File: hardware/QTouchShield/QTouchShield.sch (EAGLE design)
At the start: 114 parts, among them IC1 AT32UC3C0512CJEDEC-MS-026, U1 ARDUINO-MEGALITE

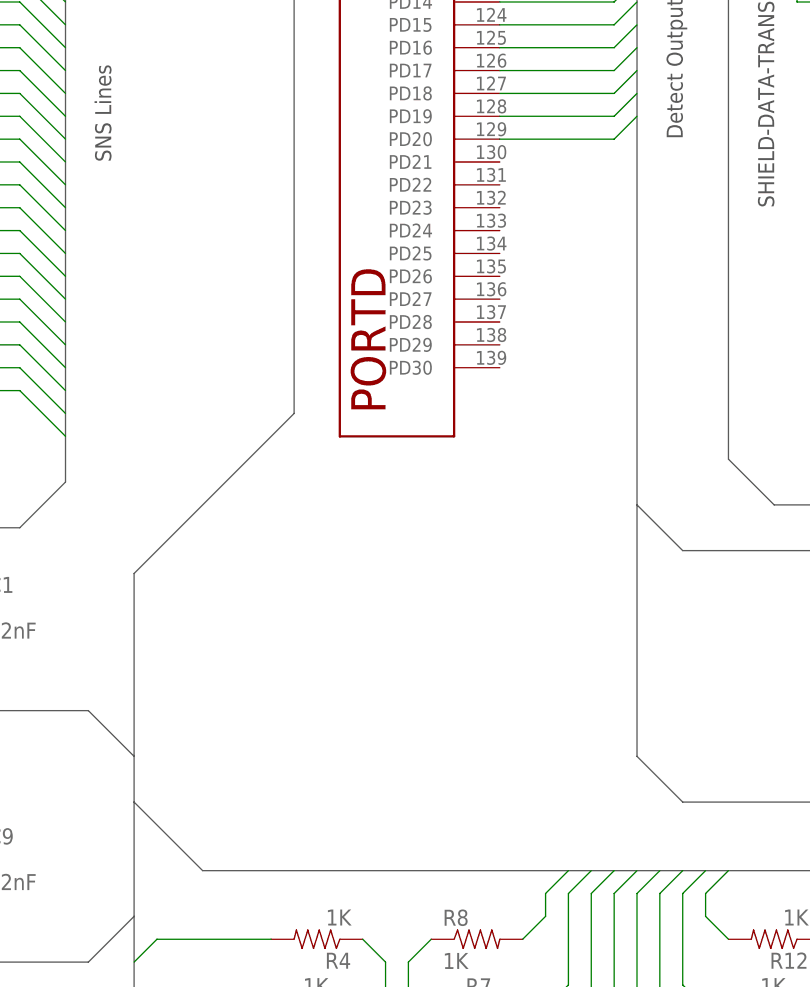
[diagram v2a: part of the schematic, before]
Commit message: Added TOUCH DATA header for data transfer to QT600 Interface Board
TOUCH DATA header added. This is the bit-banged SPI interface for
transferring debug data to the QT600 board for analysing touch data
with QTouch Studio.
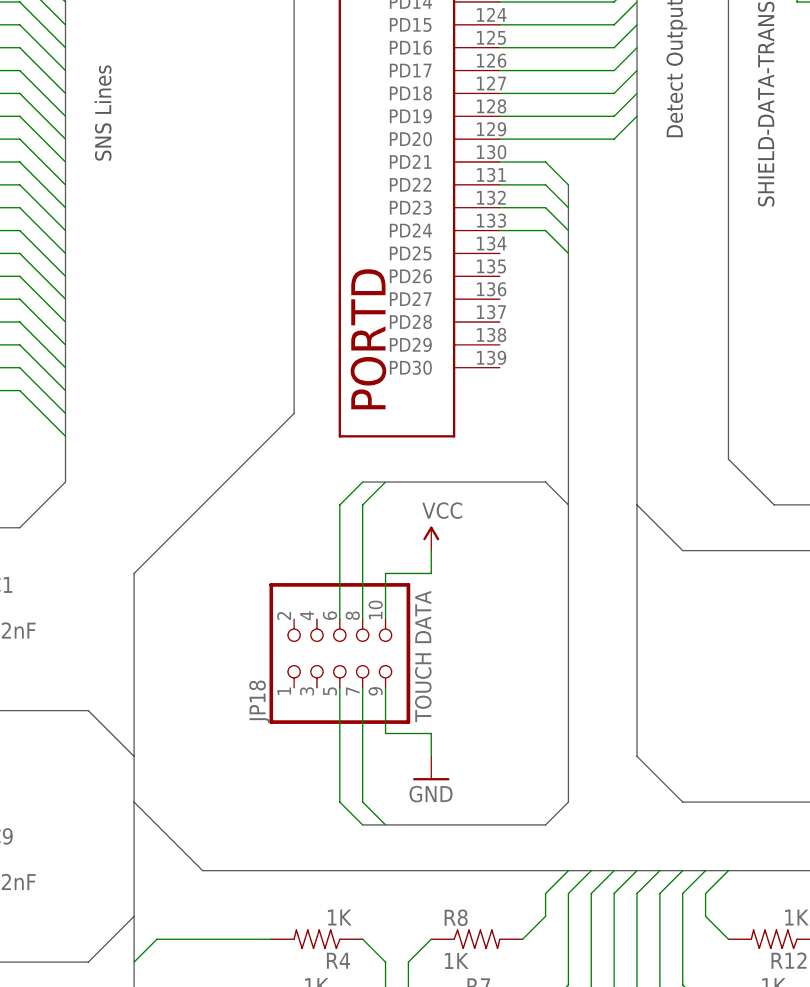
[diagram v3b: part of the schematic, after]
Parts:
- added JP18: TOUCH DATA, pinhead:PINHD-2X5
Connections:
- new net TOUCH_DATA-MISO: IC1.PD24, JP18.7
- new net TOUCH_DATA-MOSI: IC1.PD23, JP18.6
- new net TOUCH_DATA-SCK: IC1.PD22, JP18.8
- new net TOUCH_DATA-SS: IC1.PD21, JP18.5
- net GND: now also JP18.9
- net VCC: now also JP18.10
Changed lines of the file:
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@@
 <layers>
 <layer number="1" name="Top" color="4" fill="1" visible="no" active="no"/>
+<layer number="2" name="Route2" color="1" fill="3" visible="no" active="no"/>
+<layer number="3" name="Route3" color="4" fill="3" visible="no" active="no"/>
+<layer number="14" name="Route14" color="1" fill="6" visible="no" active="no"/>
+<layer number="15" name="Route15" color="4" fill="6" visible="no" active="no"/>
 <layer number="16" name="Bottom" color="1" fill="1" visible="no" active="no"/>
 <layer number="17" name="Pads" color="2" fill="1" visible="no" active="no"/>
@@
 <part name="R35" library="SparkFun" deviceset="RESISTOR" device="0805-RES" value="10K"/>
 <part name="SJ5" library="jumper" deviceset="SJ" device="" value="RESET-LINK"/>
+<part name="JP18" library="pinhead" deviceset="PINHD-2X5" device="" value="TOUCH DATA"/>
+<part name="GND9" library="SparkFun" deviceset="GND" device=""/>
+<part name="P+6" library="SparkFun" deviceset="VCC" device=""/>
 </parts>
 <sheets>
@@
 <attribute name="VALUE" x="194.31" y="40.64" size="1.778" layer="96" rot="R270"/>
 </instance>
+<instance part="JP18" gate="A" x="116.84" y="-139.7" rot="R90"/>
+<instance part="GND9" gate="1" x="127" y="-152.4"/>
+<instance part="P+6" gate="1" x="127" y="-127"/>
 </instances>
 <busses>
@@
 </segment>
 </bus>
+<bus name="TOUCH_DATA-SS,TOUCH_DATA-SCK,TOUCH_DATA-MOSI,TOUCH_DATA-MISO">
+<segment>
+<wire x1="142.24" y1="-86.36" x2="142.24" y2="-121.92" width="0.762" layer="92"/>
+<wire x1="142.24" y1="-121.92" x2="139.7" y2="-119.38" width="0.762" layer="92"/>
+<wire x1="139.7" y1="-119.38" x2="119.38" y2="-119.38" width="0.762" layer="92"/>
+<wire x1="142.24" y1="-121.92" x2="142.24" y2="-154.94" width="0.762" layer="92"/>
+<wire x1="142.24" y1="-154.94" x2="139.7" y2="-157.48" width="0.762" layer="92"/>
+<wire x1="139.7" y1="-157.48" x2="119.38" y2="-157.48" width="0.762" layer="92"/>
+</segment>
+</bus>
 </busses>
 <nets>
@@
 <wire x1="-22.86" y1="-40.64" x2="-22.86" y2="-38.1" width="0.1524" layer="91"/>
 </segment>
+<segment>
+<pinref part="GND9" gate="1" pin="GND"/>
+<wire x1="127" y1="-149.86" x2="127" y2="-147.32" width="0.1524" layer="91"/>
+<wire x1="127" y1="-147.32" x2="121.92" y2="-147.32" width="0.1524" layer="91"/>
+<pinref part="JP18" gate="A" pin="9"/>
+<wire x1="121.92" y1="-147.32" x2="121.92" y2="-142.24" width="0.1524" layer="91"/>
+</segment>
 </net>
 <net name="N$2" class="0">
@@
 <wire x1="-12.7" y1="20.32" x2="-12.7" y2="22.86" width="0.1524" layer="91"/>
 </segment>
+<segment>
+<pinref part="P+6" gate="1" pin="VCC"/>
+<wire x1="127" y1="-127" x2="127" y2="-129.54" width="0.1524" layer="91"/>
+<wire x1="127" y1="-129.54" x2="121.92" y2="-129.54" width="0.1524" layer="91"/>
+<pinref part="JP18" gate="A" pin="10"/>
+<wire x1="121.92" y1="-129.54" x2="121.92" y2="-134.62" width="0.1524" layer="91"/>
+</segment>
 </net>
 <net name="JTAG_TMS" class="0">
@@
 </segment>
 </net>
+<net name="TOUCH_DATA-SS" class="0">
+<segment>
+<wire x1="142.24" y1="-86.36" x2="139.7" y2="-83.82" width="0.1524" layer="91"/>
+<pinref part="IC1" gate="G$1" pin="PD21"/>
+<wire x1="139.7" y1="-83.82" x2="134.62" y2="-83.82" width="0.1524" layer="91"/>
+</segment>
+<segment>
+<wire x1="119.38" y1="-157.48" x2="116.84" y2="-154.94" width="0.1524" layer="91"/>
+<pinref part="JP18" gate="A" pin="5"/>
+<wire x1="116.84" y1="-154.94" x2="116.84" y2="-142.24" width="0.1524" layer="91"/>
+</segment>
+</net>
+<net name="TOUCH_DATA-SCK" class="0">
+<segment>
+<wire x1="142.24" y1="-88.9" x2="139.7" y2="-86.36" width="0.1524" layer="91"/>
+<pinref part="IC1" gate="G$1" pin="PD22"/>
+<wire x1="139.7" y1="-86.36" x2="134.62" y2="-86.36" width="0.1524" layer="91"/>
+</segment>
+<segment>
+<wire x1="121.92" y1="-119.38" x2="119.38" y2="-121.92" width="0.1524" layer="91"/>
+<pinref part="JP18" gate="A" pin="8"/>
+<wire x1="119.38" y1="-121.92" x2="119.38" y2="-134.62" width="0.1524" layer="91"/>
+</segment>
+</net>
+<net name="TOUCH_DATA-MOSI" class="0">
+<segment>
+<wire x1="142.24" y1="-91.44" x2="139.7" y2="-88.9" width="0.1524" layer="91"/>
+<pinref part="IC1" gate="G$1" pin="PD23"/>
+<wire x1="139.7" y1="-88.9" x2="134.62" y2="-88.9" width="0.1524" layer="91"/>
+</segment>
+<segment>
+<wire x1="119.38" y1="-119.38" x2="116.84" y2="-121.92" width="0.1524" layer="91"/>
+<pinref part="JP18" gate="A" pin="6"/>
+<wire x1="116.84" y1="-121.92" x2="116.84" y2="-134.62" width="0.1524" layer="91"/>
+</segment>
+</net>
+<net name="TOUCH_DATA-MISO" class="0">
+<segment>
+<wire x1="142.24" y1="-93.98" x2="139.7" y2="-91.44" width="0.1524" layer="91"/>
+<pinref part="IC1" gate="G$1" pin="PD24"/>
+<wire x1="139.7" y1="-91.44" x2="134.62" y2="-91.44" width="0.1524" layer="91"/>
+</segment>
+<segment>
+<wire x1="121.92" y1="-157.48" x2="119.38" y2="-154.94" width="0.1524" layer="91"/>
+<pinref part="JP18" gate="A" pin="7"/>
+<wire x1="119.38" y1="-154.94" x2="119.38" y2="-142.24" width="0.1524" layer="91"/>
+</segment>
+</net>
